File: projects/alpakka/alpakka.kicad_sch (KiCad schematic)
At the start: 77 parts, among them P1 Debug, P2 Endpoint, P3 Conn_01x02, Q1 Q_PMOS_DGS, U1 Raspberry_Pico, U10 ST_LSM6, U12 ST_LSM6, U2 Alpsalpine_RKJXV, U3 Alpsalpine_EC10E, U4 Alpsalpine_RKJXM, U6 PCAL6416A, U8 PCAL6416A

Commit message: mod button keepout zone
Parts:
- D1, D2, D3, D4: footprint ILO_fp:0603_d -> Diode_SMD:D_0603_1608Metric_Pad1.05x0.95mm_HandSolder; digikey# (none) -> 1830-1063-1-ND; manf (none) -> Inolux; manf# (none) -> IN-S63AT5UW
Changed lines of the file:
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@@
 			)
 		)
-		(property "Footprint" "ILO_fp:0603_d"
+		(property "Footprint" "Diode_SMD:D_0603_1608Metric_Pad1.05x0.95mm_HandSolder"
 			(at 125.73 80.01 0)
 			(effects
@@
 			)
 		)
-		(property "Description" ""
+		(property "Description" "White LED Indication - Discrete 2.8V 0603 (1608 Metric)"
 			(at 125.73 80.01 0)
 			(effects
@@
 		)
 		(property "Export" "yes"
+			(at 125.73 80.01 0)
+			(effects
+				(font
+					(size 1.27 1.27)
+				)
+				(hide yes)
+			)
+		)
+		(property "digikey#" "1830-1063-1-ND"
+			(at 125.73 80.01 0)
+			(effects
+				(font
+					(size 1.27 1.27)
+				)
+				(hide yes)
+			)
+		)
+		(property "manf" "Inolux"
+			(at 125.73 80.01 0)
+			(effects
+				(font
+					(size 1.27 1.27)
+				)
+				(hide yes)
+			)
+		)
+		(property "manf#" "IN-S63AT5UW"
 			(at 125.73 80.01 0)
 			(effects
@@
 			)
 		)
-		(property "Footprint" "ILO_fp:0603_d"
+		(property "Footprint" "Diode_SMD:D_0603_1608Metric_Pad1.05x0.95mm_HandSolder"
 			(at 125.73 83.82 0)
 			(effects
@@
 			)
 		)
-		(property "Description" ""
+		(property "Description" "White LED Indication - Discrete 2.8V 0603 (1608 Metric)"
 			(at 125.73 83.82 0)
 			(effects
@@
 		)
 		(property "Export" "yes"
+			(at 125.73 83.82 0)
+			(effects
+				(font
+					(size 1.27 1.27)
+				)
+				(hide yes)
+			)
+		)
+		(property "digikey#" "1830-1063-1-ND"
+			(at 125.73 83.82 0)
+			(effects
+				(font
+					(size 1.27 1.27)
+				)
+				(hide yes)
+			)
+		)
+		(property "manf" "Inolux"
+			(at 125.73 83.82 0)
+			(effects
+				(font
+					(size 1.27 1.27)
+				)
+				(hide yes)
+			)
+		)
+		(property "manf#" "IN-S63AT5UW"
 			(at 125.73 83.82 0)
 			(effects
@@
 			)
 		)
-		(property "Footprint" "ILO_fp:0603_d"
+		(property "Footprint" "Diode_SMD:D_0603_1608Metric_Pad1.05x0.95mm_HandSolder"
 			(at 125.73 76.2 0)
 			(effects
@@
 			)
 		)
-		(property "Description" ""
+		(property "Description" "White LED Indication - Discrete 2.8V 0603 (1608 Metric)"
 			(at 125.73 76.2 0)
 			(effects
@@
 		)
 		(property "Export" "yes"
+			(at 125.73 76.2 0)
+			(effects
+				(font
+					(size 1.27 1.27)
+				)
+				(hide yes)
+			)
+		)
+		(property "digikey#" "1830-1063-1-ND"
+			(at 125.73 76.2 0)
+			(effects
+				(font
+					(size 1.27 1.27)
+				)
+				(hide yes)
+			)
+		)
+		(property "manf" "Inolux"
+			(at 125.73 76.2 0)
+			(effects
+				(font
+					(size 1.27 1.27)
+				)
+				(hide yes)
+			)
+		)
+		(property "manf#" "IN-S63AT5UW"
 			(at 125.73 76.2 0)
 			(effects
@@
 			)
 		)
-		(property "Footprint" "ILO_fp:0603_d"
+		(property "Footprint" "Diode_SMD:D_0603_1608Metric_Pad1.05x0.95mm_HandSolder"
 			(at 125.73 72.39 0)
 			(effects
@@
 			)
 		)
-		(property "Description" ""
+		(property "Description" "White LED Indication - Discrete 2.8V 0603 (1608 Metric)"
 			(at 125.73 72.39 0)
 			(effects
@@
 			(at 125.73 72.39 0)
 			(effects
+				(font
+					(size 1.27 1.27)
+				)
+				(hide yes)
+			)
+		)
+		(property "digikey#" "1830-1063-1-ND"
+			(at 125.73 72.39 0)
+			(effects
+				(font
+					(size 1.27 1.27)
+				)
+				(hide yes)
+			)
+		)
+		(property "manf" "Inolux"
+			(at 125.73 72.39 0)
+			(effects
+				(font
+					(size 1.27 1.27)
+				)
+				(hide yes)
+			)
+		)
+		(property "manf#" "IN-S63AT5UW"
+			(at 125.73 72.39 0)
+			(effects

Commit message: add 3d model of the debug connector
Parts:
- P1: manf (none) -> JST Commercial; manf# (none) -> S4B-PH-SM4-K-TB(LF)(SN); mouser# (none) -> 306-S4BPHSM4KTBLFSN
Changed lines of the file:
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@@
 			)
 		)
-		(property "Datasheet" ""
+		(property "Datasheet" "https://www.inolux-corp.com/datasheet/SMDLED/Mono%20Color%20Top%20View/IN-S63AT%20Series_V1.4.pdf"
 			(at 125.73 80.01 0)
 			(effects
@@
 			)
 		)
-		(property "Datasheet" ""
+		(property "Datasheet" "https://www.inolux-corp.com/datasheet/SMDLED/Mono%20Color%20Top%20View/IN-S63AT%20Series_V1.4.pdf"
 			(at 125.73 83.82 0)
 			(effects
@@
 			)
 		)
-		(property "Datasheet" ""
+		(property "Datasheet" "https://www.inolux-corp.com/datasheet/SMDLED/Mono%20Color%20Top%20View/IN-S63AT%20Series_V1.4.pdf"
 			(at 125.73 76.2 0)
 			(effects
@@
 			)
 		)
-		(property "Datasheet" ""
+		(property "Datasheet" "https://www.inolux-corp.com/datasheet/SMDLED/Mono%20Color%20Top%20View/IN-S63AT%20Series_V1.4.pdf"
 			(at 125.73 72.39 0)
 			(effects
@@
 			)
 		)
-		(property "Datasheet" ""
+		(property "Datasheet" "https://tech.alpsalpine.com/e/products/detail/RKJXV122400R/"
 			(at 90.17 69.85 0)
 			(effects
@@
 			)
 		)
-		(property "Description" ""
+		(property "Description" "JST Automotive Connectors"
 			(at 132.08 31.75 0)
 			(effects
@@
 			(at 132.08 31.75 0)
 			(effects
+				(font
+					(size 1.27 1.27)
+				)
+				(hide yes)
+			)
+		)
+		(property "manf" "JST Commercial"
+			(at 132.08 31.75 0)
+			(effects
+				(font
+					(size 1.27 1.27)
+				)
+				(hide yes)
+			)
+		)
+		(property "manf#" " S4B-PH-SM4-K-TB(LF)(SN)"
+			(at 132.08 31.75 0)
+			(effects
+				(font
+					(size 1.27 1.27)
+				)
+				(hide yes)
+			)
+		)
+		(property "mouser#" "306-S4BPHSM4KTBLFSN"
+			(at 132.08 31.75 0)
+			(effects

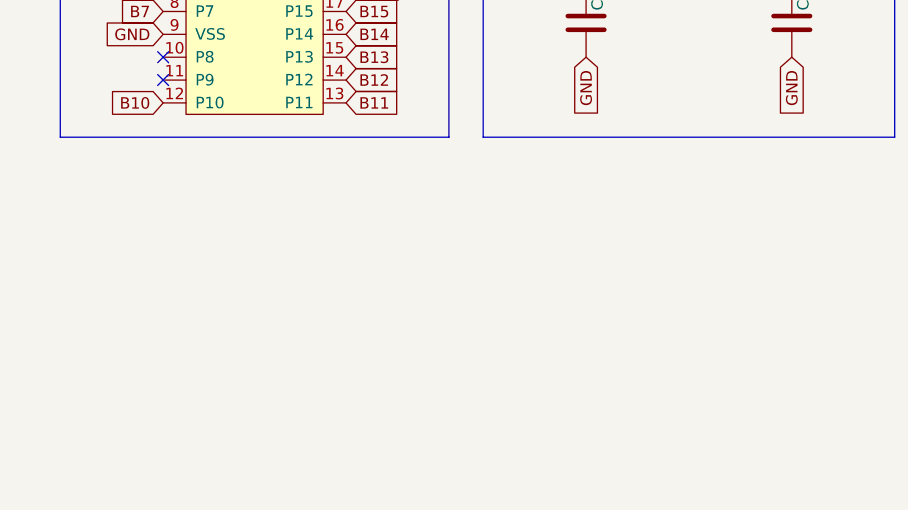
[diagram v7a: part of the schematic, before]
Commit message: add Rpi Pico 3d model, also other mods
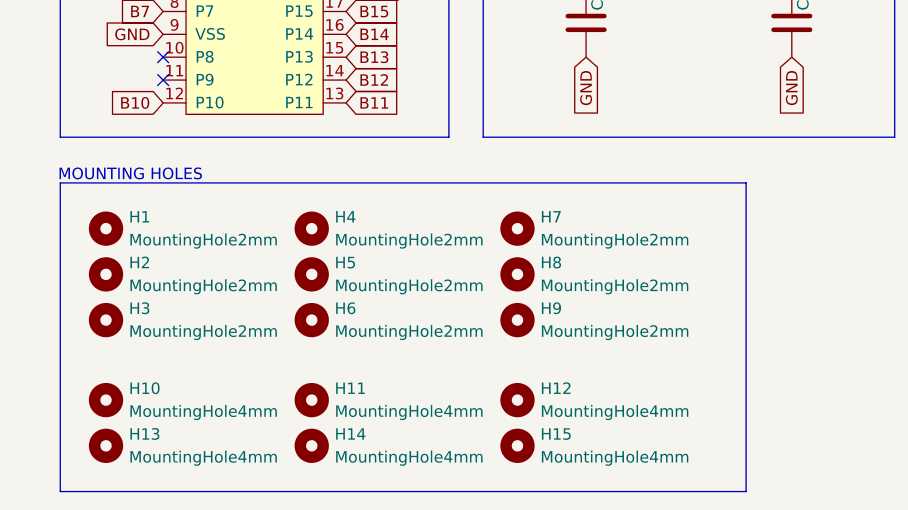
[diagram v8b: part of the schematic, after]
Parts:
- added H1, H2, H3, H4, H5, H6, H7, H8, H9: MountingHole2mm, ILO_fp:NPTH_2mm, symbol Mechanical:MountingHole
- added H10, H11, H12, H13, H14, H15: MountingHole4mm, ILO_fp:NPTH_4mm, symbol Mechanical:MountingHole
- C1, C2, C3, C4, C5, C6: value C -> 0.1µF
- Q1: digikey# (none) -> DMG2305UX-7DICT-ND; manf (none) -> Diodes Incorporated; manf# (none) -> DMG2305UX-7
- R1, R2, R3, R4: value R -> 20Ω
- R6: value R6 -> 510kΩ
- TP10, TP101, TP102, TP103, TP104, TP11, TP12, TP14, TP15, TP16, TP19, TP20, TP201, TP202, TP203, TP204, TP24, TP25, TP26, TP3, TP31, TP32, TP33, TP35, TP36, TP4, TP5, TP6, TP7, TP9: now left out of the parts list
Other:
- note added: "MOUNTING HOLES"
